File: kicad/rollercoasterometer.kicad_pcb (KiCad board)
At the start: 2 copper layers, 61 x 94 mm, 130 parts, among them J101 USB_C_Receptacle, J120 STANDOFF, J125 STANDOFF, J127 STANDOFF, J129 STANDOFF, J1401 USB_C_Receptacle, J1402 USB_C_Receptacle, J1601 USB_C_Receptacle, J1602 USB_C_Receptacle, J401 SMA, Q2001 NMOS, Q3101 NMOS, Q801 NMOS, U1001 TCR2EF 1.8V, U104 Teensy4.1, U1101 BMM150, U1201 ICM-42688, U1301 ICM-42688, U1801 TLE493D-W2B6, U1901 TCR2EF 1.8V, U201 ICM-42688, U2101 ICM-42688, U2201 BMM150, U2401 AK09918, U2501 BMP384, U2701 ICM-42688, U2801 TLE493D-W2B6, U2901 BMP384, U3001 TCR2EF 1.8V, U301 NSP4201MR6, U3201 ICM-42688, U3301 BMM150, U3401 AK09918, U401 ZED_F9R, U501 TCR2EF 3.3V, U601 AK09918, U704 TLE493D-W2B6, U901 BMP384

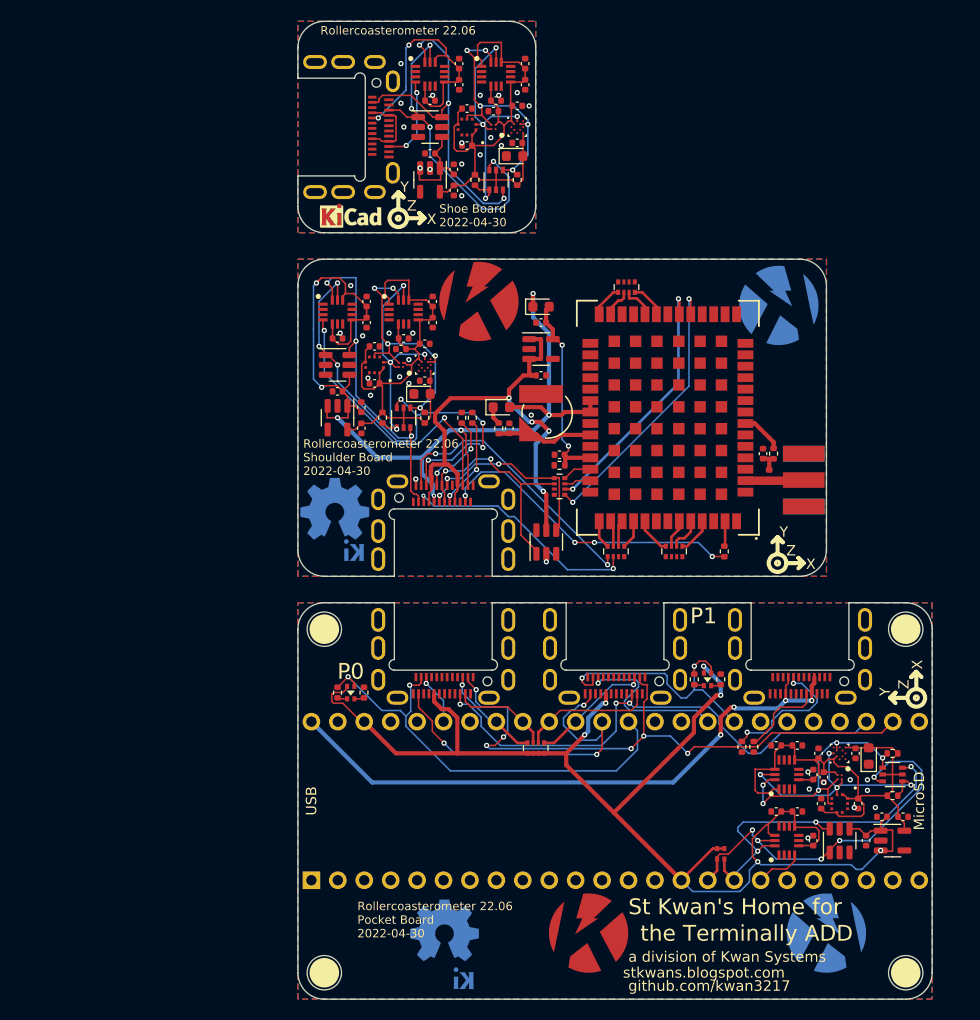
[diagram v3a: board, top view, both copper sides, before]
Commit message: Updated PCB
Updated ESD diode and routing of lines through it. Added corner silkscreen marks around all LGA/BGA parts, to allow easier inspection of placement before reflow.
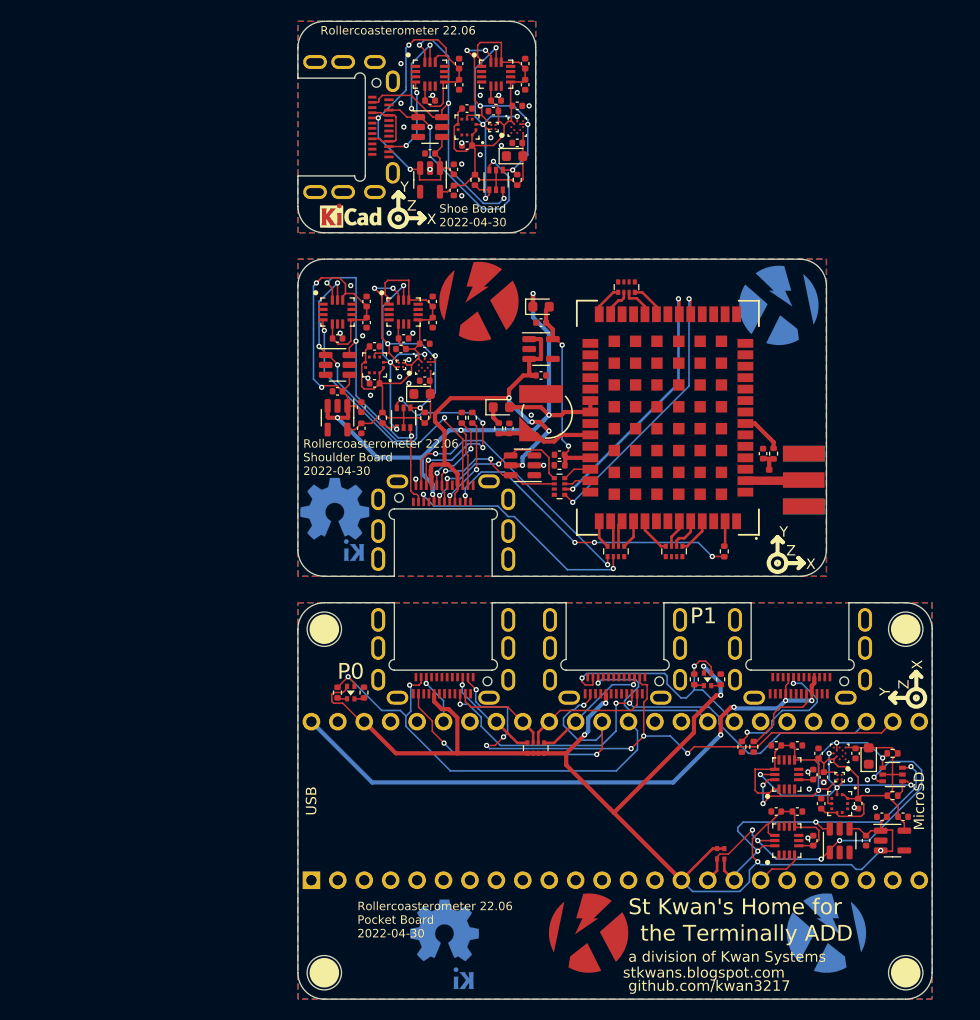
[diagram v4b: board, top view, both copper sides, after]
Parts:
- moved U301 7.71 mm to (97.8, 103.6), turned to 180 degrees
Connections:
- U301 pad 1: /Shoulder/Q_D+ -> unconnected-(U301-Pad1)
- U301 pad 6: unconnected-(U301-Pad6) -> /Shoulder/Q_D+
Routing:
- net /Shoulder/Q_D+: track 22.7 -> 15.4 mm
- net /Shoe/Q_3V3: track 34.5 -> 41.7 mm
- net /Shoulder/Q_VBUS: track 48.0 -> 41.3 mm
- net /Shoulder/Q_D-: track 20.5 -> 16.6 mm
- net /Shoulder/Q_GND: track 0.77 -> 0.00 mm

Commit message: Updated PCB to follow schematic changes
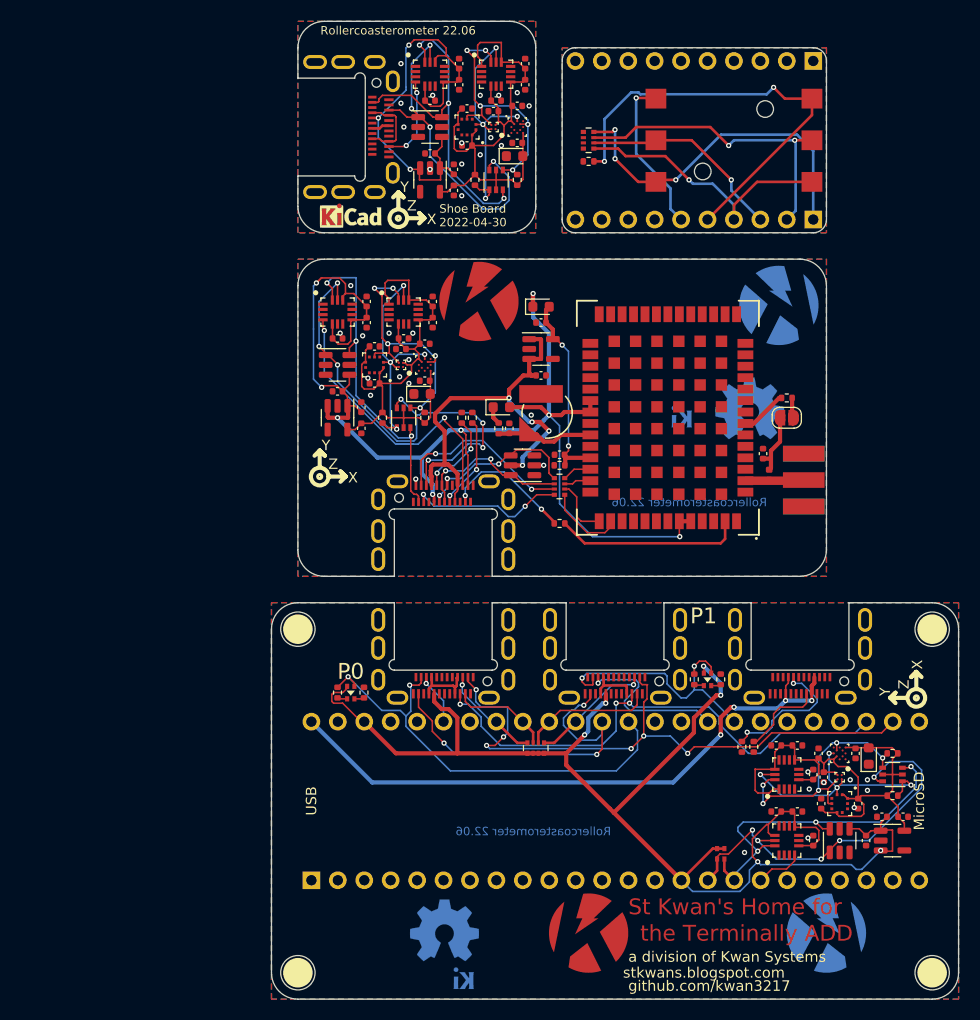
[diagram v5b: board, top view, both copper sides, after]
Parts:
- removed R408, R409, R410: 27, KwanSystems:R_Array_Convex_4x0402
- added J3501: Conn_01x10, Connector_PinHeader_2.54mm:PinHeader_1x10_P2.54mm_Vertical, B.Cu at (125.7, 80.0)
- added J3502: Conn_01x10, Connector_PinHeader_2.54mm:PinHeader_1x10_P2.54mm_Vertical, B.Cu at (125.7, 64.8)
- added J402: SolderJumper_2_Open, Jumper:SolderJumper-2_P1.3mm_Open_RoundedPad1.0x1.5mm, F.Cu at (123.2, 99.1)
- added R3501: 2.2k, KwanSystems:R_Array_Convex_4x0402, F.Cu at (104.1, 72.4)
- added R3502: 5.1k, Resistor_SMD:R_0402_1005Metric, F.Cu at (104.1, 74.4)
- added S3501: JS5208, KwanSystems:JS5208, F.Cu at (118.1, 72.4)
- R116, R138: value 10k -> 2.2k
- R1402, R1602: value 1k -> 1.5k
- U301: value NSP4201MR6 -> USBLC6-4SC6
- moved G305 44.8 mm to (78.3, 104.7)
- moved G304 41.0 mm to (119.6, 98.2)
- moved G303 34.0 mm to (111.3, 99.1)
- moved R453 16.1 mm to (101.3, 109.2), turned to 180 degrees
- moved R407 5.50 mm to (123.2, 97.2), turned to 180 degrees
- moved J120 2.54 mm to (76.2, 119.4)
- moved J125 2.54 mm to (76.2, 152.4)
- moved J127 2.54 mm to (137.2, 119.4)
- moved J129 2.54 mm to (137.2, 152.4)
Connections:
- C401 pad 1: /Shoulder/GPS Rover/V_RF- -> /Shoulder/GPS Rover/V_RF--
- J1401 pad A9: (no net) -> unconnected-(J1401-PadA4)
- J1401 pad B4: (no net) -> unconnected-(J1401-PadA4)
- J1401 pad B9: (no net) -> unconnected-(J1401-PadA4)
- J1601 pad A9: (no net) -> unconnected-(J1601-PadA4)
- J1601 pad B4: (no net) -> unconnected-(J1601-PadA4)
- J1601 pad B9: (no net) -> unconnected-(J1601-PadA4)
- L401 pad 2: /Shoulder/GPS Rover/V_RF- -> /Shoulder/GPS Rover/V_RF--
- R439 pad 3: /Shoulder/GPS Rover/RTK -> /Shoulder/Q_TX_GPS
- R439 pad 4: /Shoulder/GPS Rover/GEOFENCE -> /Shoulder/Q_RX_GPS
- R439 pad 5: /Shoulder/GPS Rover/GEOFENCE_STAT- -> /Shoulder/GPS Rover/RX/MOSI-
- R439 pad 6: /Shoulder/GPS Rover/RTK_STAT- -> /Shoulder/GPS Rover/TX/MISO-
- U104 pad 12: unconnected-(U104-Pad12) -> /TV_~{CS}
- U104 pad 13: unconnected-(U104-Pad13) -> /TV_DA
- U104 pad 19: unconnected-(U104-Pad19) -> /BTN_3V3
- U104 pad 20: unconnected-(U104-Pad20) -> /UP
- U104 pad 21: unconnected-(U104-Pad21) -> /DOWN
- U104 pad 22: unconnected-(U104-Pad22) -> /LEFT
- U104 pad 23: unconnected-(U104-Pad23) -> /RIGHT
- U104 pad 24: unconnected-(U104-Pad24) -> /PUSH
- U104 pad 35: unconnected-(U104-Pad35) -> /TV_SCK
- U104 pad 4: unconnected-(U104-Pad4) -> /TV_~{RST}
- U104 pad 7: unconnected-(U104-Pad7) -> /TV_D/~{C}
- U401 pad 19: /Shoulder/GPS Rover/GEOFENCE_STAT- -> unconnected-(U401-Pad19)
- U401 pad 20: /Shoulder/GPS Rover/RTK_STAT- -> unconnected-(U401-Pad20)
- U401 pad 22: /Shoulder/GPS Rover/WT- -> /Shoulder/Q_GND
- U401 pad 23: /Shoulder/GPS Rover/DIR- -> /Shoulder/Q_GND
- U401 pad 26: /Shoulder/GPS Rover/RX2- -> /Shoulder/Q_GND
- U401 pad 27: /Shoulder/GPS Rover/TX2- -> unconnected-(U401-Pad27)
- U401 pad 44: /Shoulder/GPS Rover/SDA/~{CS}- -> unconnected-(U401-Pad44)
- U401 pad 45: /Shoulder/GPS Rover/SCL/SCK- -> unconnected-(U401-Pad45)
- U401 pad 46: /Shoulder/GPS Rover/TX_READY- -> unconnected-(U401-Pad46)
- U401 pad 47: /Shoulder/GPS Rover/D_SEL -> unconnected-(U401-Pad47)
- U401 pad 49: /Shoulder/GPS Rover/~{RESET}- -> /Shoulder/Q_3V3
- U401 pad 50: /Shoulder/GPS Rover/~{SAFEBOOT}- -> /Shoulder/Q_3V3
- U401 pad 51: /Shoulder/GPS Rover/EXT_INT- -> unconnected-(U401-Pad51)
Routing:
- net /Joystick/UP: track 0.00 -> 42.7 mm, vias 0 -> 2
- net /Joystick/PUSH: track 0.00 -> 34.1 mm, vias 0 -> 3
- net /Joystick/RIGHT: track 0.00 -> 30.3 mm, vias 0 -> 2
- net /Joystick/DOWN: track 0.00 -> 26.9 mm, vias 0 -> 1
- net /Shoulder/GPS Rover/GEOFENCE_STAT-: track 26.8 -> 0.00 mm, vias 2 -> 0
- net /Shoulder/GPS Rover/RTK_STAT-: track 24.8 -> 0.00 mm, vias 2 -> 0
- net /Shoulder/Q_3V3: track 95.0 -> 119.4 mm, vias 7 -> 8
- net /Joystick/LEFT: track 0.00 -> 19.9 mm, vias 0 -> 1
- net /Shoulder/Q_PPS: track 30.3 -> 12.7 mm, vias 4 -> 2
- net /Shoulder/GPS Rover/TIMEPULSE-: track 2.38 -> 18.1 mm
- net /Joystick/3V3: track 0.00 -> 15.4 mm, vias 0 -> 1
- net /Shoulder/Q_TX_GPS: track 26.8 -> 17.9 mm
- net /Shoulder/Q_RX_GPS: track 22.9 -> 14.8 mm
- net /Shoulder/GPS Rover/V_RF--: track 0.00 -> 6.19 mm
- net unconnected-(J1401-PadA4): track 0.00 -> 5.72 mm
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- added copper zone on B.Cu, net /Joystick/BTN_GND
- added copper zone on F.Cu, net /Joystick/BTN_GND
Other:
- board size 61 x 94 mm -> 66 x 94 mm
- board text added: "Designed with"
- board text added: "Pocket Board 2022-04-30"
- board text added: "Shoulder Board 2022-04-30"
- board text removed: "Rollercoasterometer 22.06 Pocket Board 2022-04-30"
- board text removed: "Rollercoasterometer 22.06 Shoulder Board 2022-04-30"

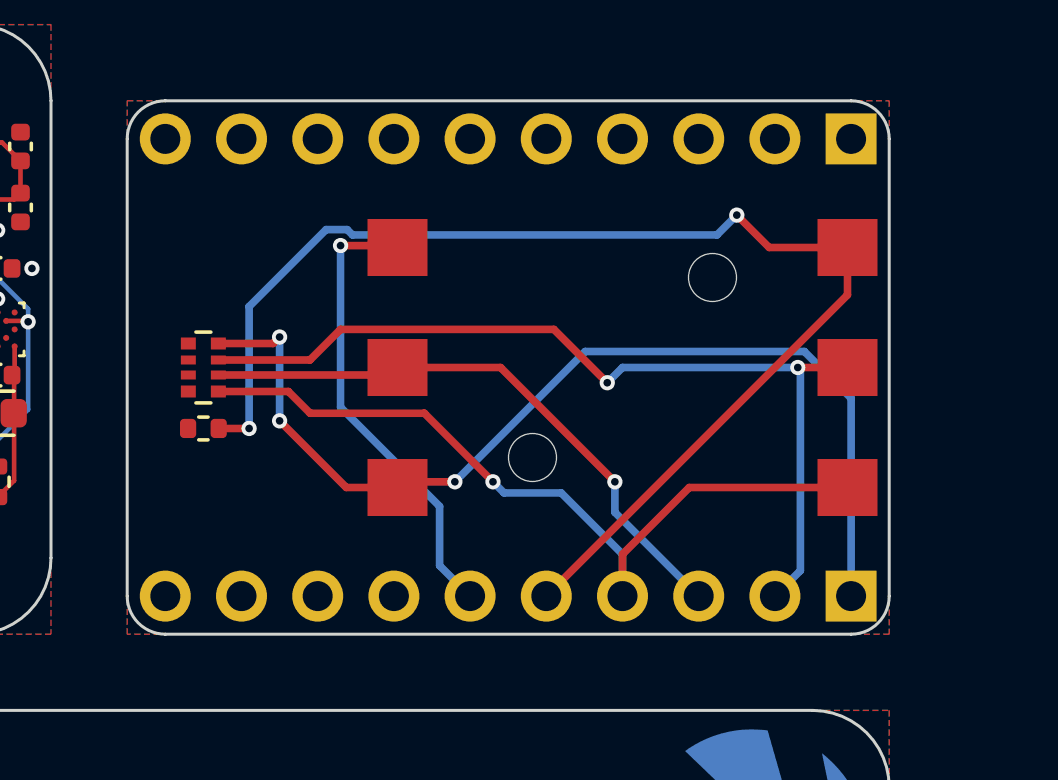
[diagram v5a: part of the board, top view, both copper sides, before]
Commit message: Replaced JS5208 with smaller JS1400
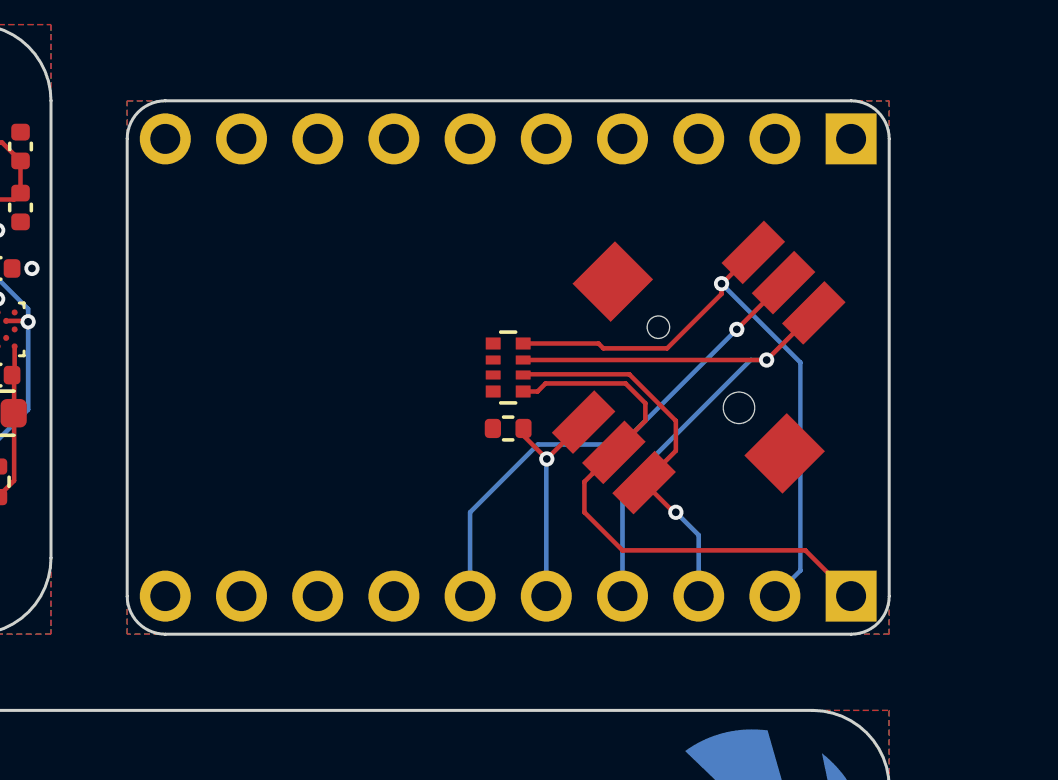
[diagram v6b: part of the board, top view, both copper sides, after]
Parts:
- S3501: value JS5208 -> JS1400; footprint KwanSystems:JS5208 -> KwanSystems:JS1400
- moved R3501 10.2 mm to (114.3, 72.4)
- moved R3502 10.2 mm to (114.3, 74.4)
- moved S3501 2.54 mm to (120.7, 72.4), turned to 45 degrees
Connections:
- net /Joystick/BTN_GND renamed /Joystick/Q_GND
- J3501 pad 1: /Joystick/PUSH -> /Joystick/Q_PUSH
- J3501 pad 2: /Joystick/RIGHT -> /Joystick/Q_UP
- J3501 pad 3: /Joystick/LEFT -> /Joystick/Q_DOWN
- J3501 pad 4: /Joystick/DOWN -> /Joystick/Q_RIGHT
- J3501 pad 5: /Joystick/UP -> /Joystick/Q_LEFT
- J3501 pad 6: /Joystick/3V3 -> /Joystick/Q_3V3
- R3501 pad 5: /Joystick/DOWN -> /Joystick/Q_PUSH
- R3501 pad 6: /Joystick/LEFT -> /Joystick/Q_DOWN
- R3501 pad 7: /Joystick/RIGHT -> /Joystick/Q_RIGHT
- R3501 pad 8: /Joystick/PUSH -> /Joystick/Q_UP
- R3502 pad 2: /Joystick/UP -> /Joystick/Q_LEFT
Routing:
- net /Joystick/UP: track 42.7 -> 0.00 mm, vias 2 -> 0
- net /Joystick/PUSH: track 34.1 -> 0.00 mm, vias 3 -> 0
- net /Joystick/RIGHT: track 30.3 -> 0.00 mm, vias 2 -> 0
- net /Joystick/DOWN: track 26.9 -> 0.00 mm, vias 1 -> 0
- net /Joystick/Q_UP: track 0.00 -> 21.1 mm, vias 0 -> 1
- net /Joystick/Q_RIGHT: track 0.00 -> 20.5 mm, vias 0 -> 1
- net /Joystick/Q_PUSH: track 0.00 -> 20.0 mm
- net /Joystick/LEFT: track 19.9 -> 0.00 mm, vias 1 -> 0
- net /Joystick/Q_3V3: track 0.00 -> 16.4 mm, vias 0 -> 1
- net /Joystick/3V3: track 15.4 -> 0.00 mm, vias 1 -> 0
- net /Joystick/Q_DOWN: track 0.00 -> 12.8 mm, vias 0 -> 1
- net /Joystick/Q_LEFT: track 0.00 -> 7.65 mm, vias 0 -> 1
